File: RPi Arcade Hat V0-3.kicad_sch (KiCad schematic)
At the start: 100 parts, among them J1 Raspberry_Pi_2_3, J10 Coin/Note Input, J11 +24V IN, J12 +12V OUT, J13 Player 1, J14 Player 2, J15 Player 3, J16 Player 4, J19 Coin Counter, J2 Player 1, J3 Player 2, J4 Player 3, J5 Player 4, J6 Spare, J7 +24V OUT, Q1 BC847, Q10 BC847, Q11 BC847, Q12 BC847, Q13 BC847, Q14 BC847, Q15 BC847, Q16 BC847, Q2 BC847, Q3 BC847, Q4 BC847, Q5 BC847, Q6 BC847, Q7 BC847, Q8 BC847, Q9 BC847, U1 SN74HC32N, U10 NE555DR, U12 SN74HC08N, U13 NE555DR, U14 SN74HC74N, U18 SN74HC08N, U3 LM2595S-12

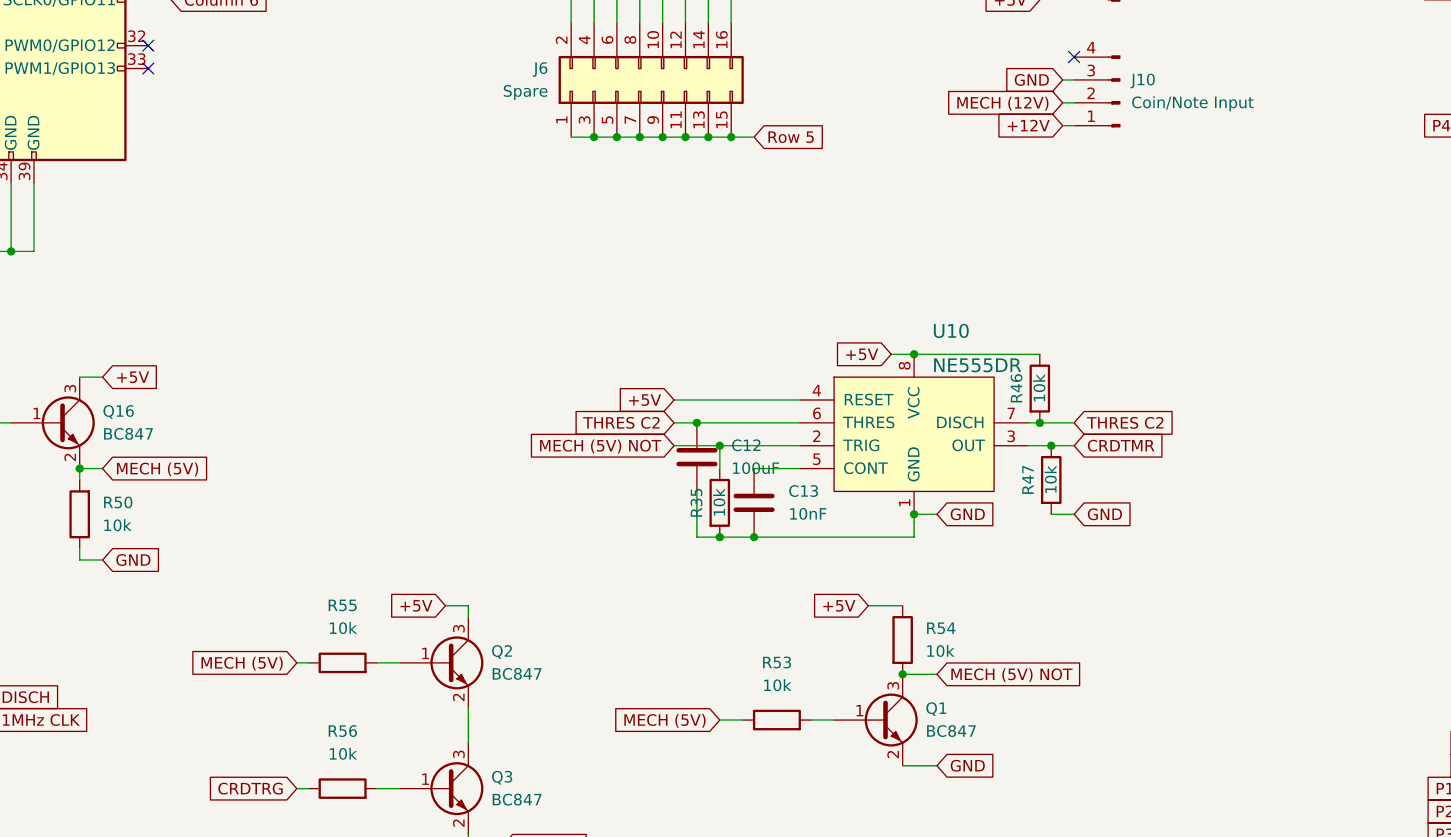
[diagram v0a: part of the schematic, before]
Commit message: Error fixed
Found a wiring error in the circuit for the credit input, had it wired for NC logic (Active High), when should've been NO(Active Low)
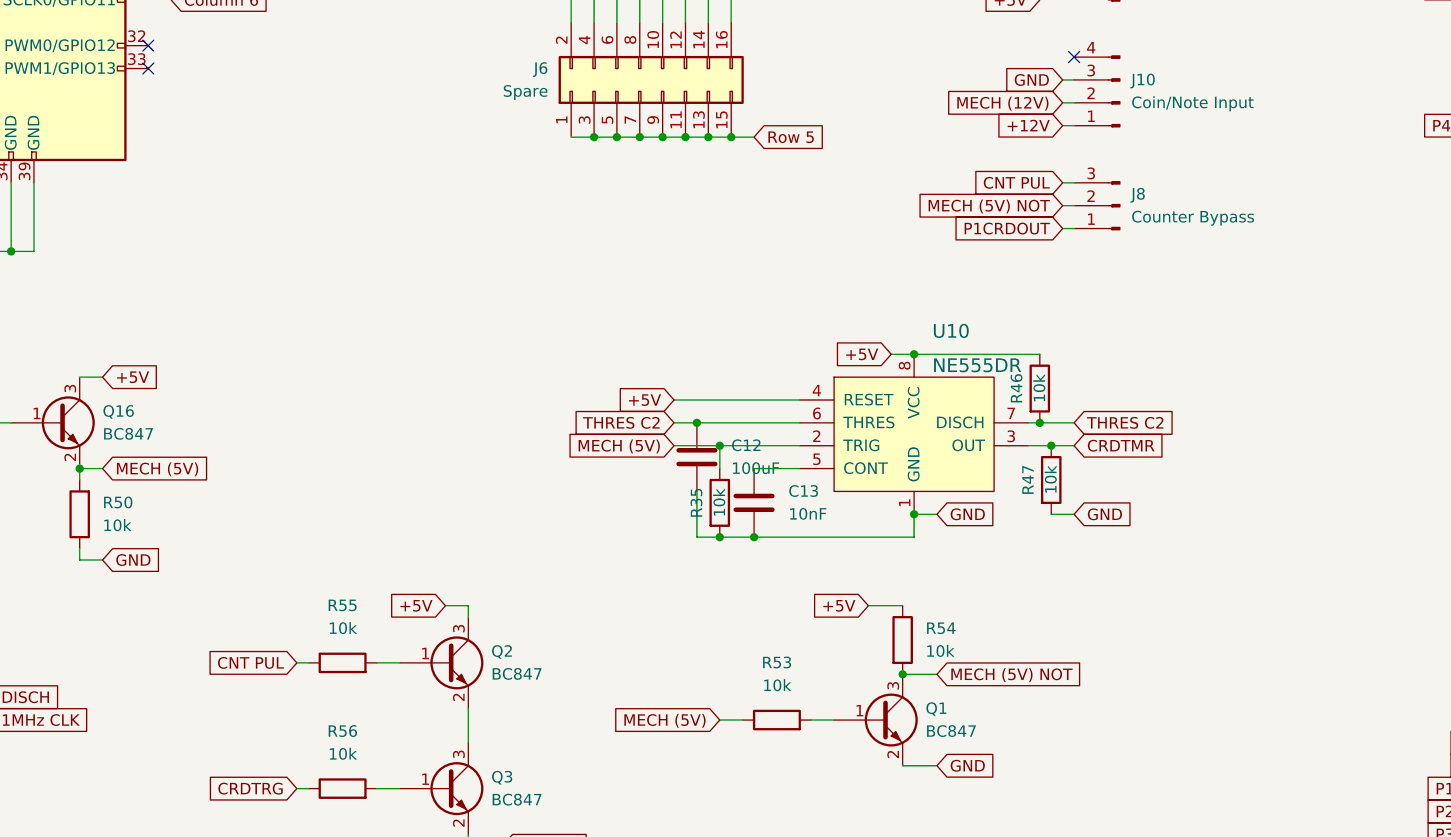
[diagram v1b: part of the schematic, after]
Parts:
- added J8: Counter Bypass, Connector_PinHeader_2.54mm:PinHeader_1x03_P2.54mm_Vertical, symbol Connector:Conn_01x03_Male
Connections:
- net MECH (5V): now also R35.1, U10.2 (TRIG); no longer R55.1
- net MECH (5V) NOT: now also J8.2 (Pin_2); no longer R35.1, U10.2 (TRIG)
- net P1CRDOUT: now also J8.1 (Pin_1)
- new net CNT PUL: J8.3 (Pin_3), R55.1
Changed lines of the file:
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@@
     (stroke (width 0) (type default) (color 0 0 0 0))
   )
+  (wire (pts (xy 170.18 87.63) (xy 171.45 87.63))
+    (stroke (width 0) (type default) (color 0 0 0 0))
+  )
   (wire (pts (xy 167.64 64.77) (xy 171.45 64.77))
     (stroke (width 0) (type default) (color 0 0 0 0))
@@
     (stroke (width 0) (type default) (color 0 0 0 0))
   )
+  (wire (pts (xy 170.18 90.17) (xy 171.45 90.17))
+    (stroke (width 0) (type default) (color 0 0 0 0))
+  )
   (wire (pts (xy 347.98 116.84) (xy 360.68 116.84))
     (stroke (width 0) (type default) (color 0 0 0 0))
@@
     (stroke (width 0) (type default) (color 0 0 0 0))
   )
+  (wire (pts (xy 170.18 85.09) (xy 171.45 85.09))
+    (stroke (width 0) (type default) (color 0 0 0 0))
+  )
   (wire (pts (xy 19.05 142.24) (xy 22.86 142.24))
     (stroke (width 0) (type default) (color 0 0 0 0))
@@
     )
   )
-  (global_label "MECH (5V)" (shape input) (at 85.09 138.43 180) (fields_autoplaced)
+  (global_label "CNT PUL" (shape input) (at 85.09 138.43 180) (fields_autoplaced)
     (effects (font (size 1.27 1.27)) (justify right))
-    (property "Intersheet References" "${INTERSHEET_REFS}" (id 0) (at 72.5169 138.3506 0)
+    (property "Intersheet References" "${INTERSHEET_REFS}" (id 0) (at 74.5126 138.3506 0)
       (effects (font (size 1.27 1.27)) (justify right) hide)
     )
@@
     )
   )
+  (global_label "P1CRDOUT" (shape input) (at 170.18 90.17 180) (fields_autoplaced)
+    (effects (font (size 1.27 1.27)) (justify right))
+    (property "Intersheet References" "${INTERSHEET_REFS}" (id 0) (at 157.8488 90.0906 0)
+      (effects (font (size 1.27 1.27)) (justify right) hide)
+    )
+  )
   (global_label "Column 6" (shape input) (at 128.27 64.77 90) (fields_autoplaced)
     (effects (font (size 1.27 1.27)) (justify left))
@@
     )
   )
+  (global_label "MECH (5V) NOT" (shape input) (at 170.18 87.63 180) (fields_autoplaced)
+    (effects (font (size 1.27 1.27)) (justify right))
+    (property "Intersheet References" "${INTERSHEET_REFS}" (id 0) (at 153.0107 87.5506 0)
+      (effects (font (size 1.27 1.27)) (justify right) hide)
+    )
+  )
+  (global_label "CNT PUL" (shape input) (at 170.18 85.09 180) (fields_autoplaced)
+    (effects (font (size 1.27 1.27)) (justify right))
+    (property "Intersheet References" "${INTERSHEET_REFS}" (id 0) (at 159.6026 85.0106 0)
+      (effects (font (size 1.27 1.27)) (justify right) hide)
+    )
+  )
   (global_label "1MHz CLK" (shape input) (at 50.8 170.18 180) (fields_autoplaced)
     (effects (font (size 1.27 1.27)) (justify right))
@@
     )
   )
-  (global_label "MECH (5V) NOT" (shape input) (at 127 114.3 180) (fields_autoplaced)
+  (global_label "MECH (5V)" (shape input) (at 127 114.3 180) (fields_autoplaced)
     (effects (font (size 1.27 1.27)) (justify right))
-    (property "Intersheet References" "${INTERSHEET_REFS}" (id 0) (at 109.8307 114.2206 0)
+    (property "Intersheet References" "${INTERSHEET_REFS}" (id 0) (at 114.4269 114.2206 0)
       (effects (font (size 1.27 1.27)) (justify right) hide)
     )
@@
     (pin "3")
   )
+  (symbol (lib_id "Connector:Conn_01x03_Male") (at 176.53 87.63 180) (unit 1)
+    (in_bom yes) (on_board yes) (fields_autoplaced)
+    (property "Reference" "J8" (id 0) (at 177.8 86.3599 0)
+      (effects (font (size 1.27 1.27)) (justify right))
+    )
+    (property "Value" "Counter Bypass" (id 1) (at 177.8 88.8999 0)
+      (effects (font (size 1.27 1.27)) (justify right))
+    )
+    (property "Footprint" "Connector_PinHeader_2.54mm:PinHeader_1x03_P2.54mm_Vertical" (id 2) (at 176.53 87.63 0)
+      (effects (font (size 1.27 1.27)) hide)
+    )
+    (property "Datasheet" "~" (id 3) (at 176.53 87.63 0)
+      (effects (font (size 1.27 1.27)) hide)
+    )
+    (pin "1")
+    (pin "2")
+    (pin "3")
+  )
   (symbol (lib_id "Device:R") (at 364.49 204.47 270) (unit 1)
     (in_bom yes) (on_board yes)
@@
       (reference "J7") (unit 1) (value "+24V OUT") (footprint "Connector_BarrelJack:BarrelJack_Horizontal")
     )
+    (path "/99f3a2a9-105b-4689-89d1-d927f017b118"
+      (reference "J8") (unit 1) (value "Counter Bypass") (footprint "Connector_PinHeader_2.54mm:PinHeader_1x03_P2.54mm_Vertical")
+    )
     (path "/756d0bc8-3ce9-46a9-a193-19f27b940ff1"
